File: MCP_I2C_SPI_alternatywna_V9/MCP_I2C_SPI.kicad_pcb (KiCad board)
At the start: 2 copper layers, 97.7 x 99.8 mm, 42 parts, among them J1 GPA, J10 VCC, J11 GND, J12 I2C, J13 Interrupt0, J14 A2, J15 A1, J16 A0, J17 SDA, J18 SCK, J19 INTA, J2 GPB, J20 INTB, J21 V0, J22 Ext, J23 SPI, J24 InterruptS, J25 A2, J27 GPB, J28 GPA, J29 A1, J3 Data, J31 A0, J32 INTA, J33 INTB, J4 Control, J5 Zlacze_LCD, J6 VSS, J65 SIL7, J66 SIL5, J7 K, J8 VDD, J9 A, U1 MCP23017_SP, U2 MCP23017_SP

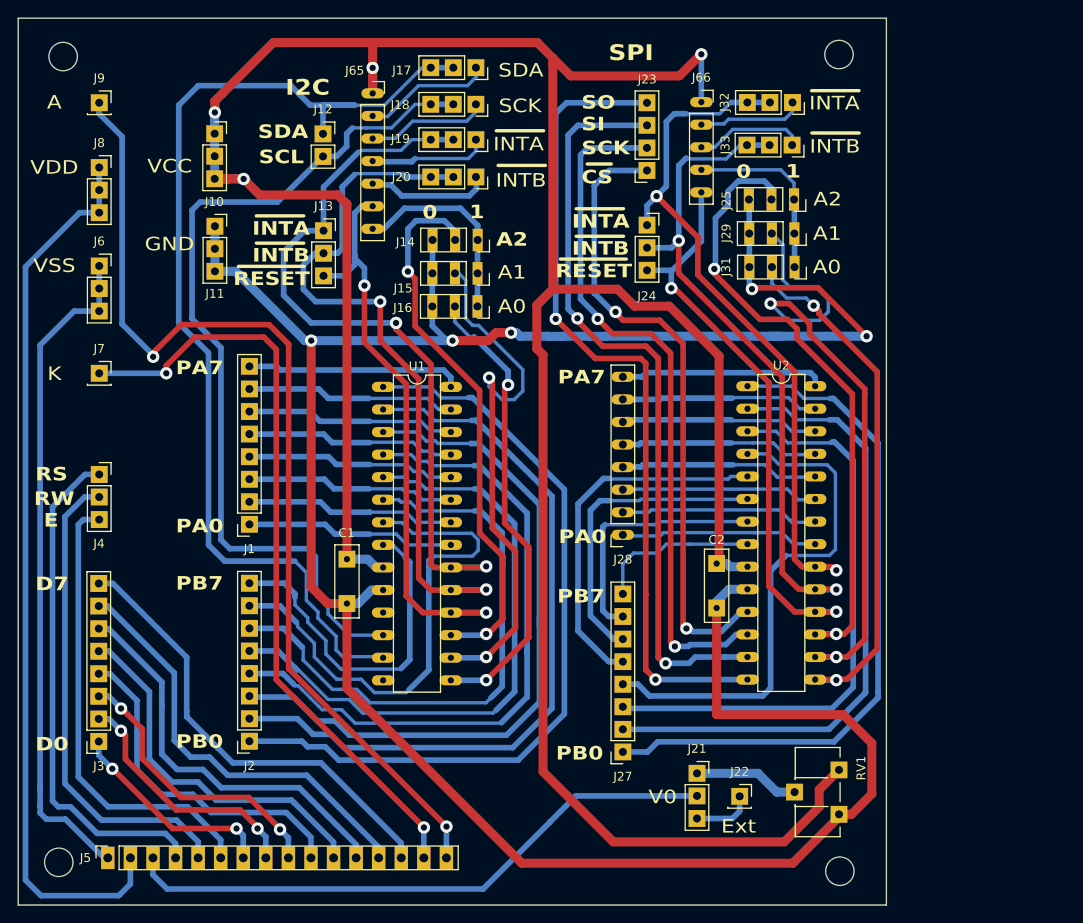
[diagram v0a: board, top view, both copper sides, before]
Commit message: MCP_I2C_SPI PCB V9
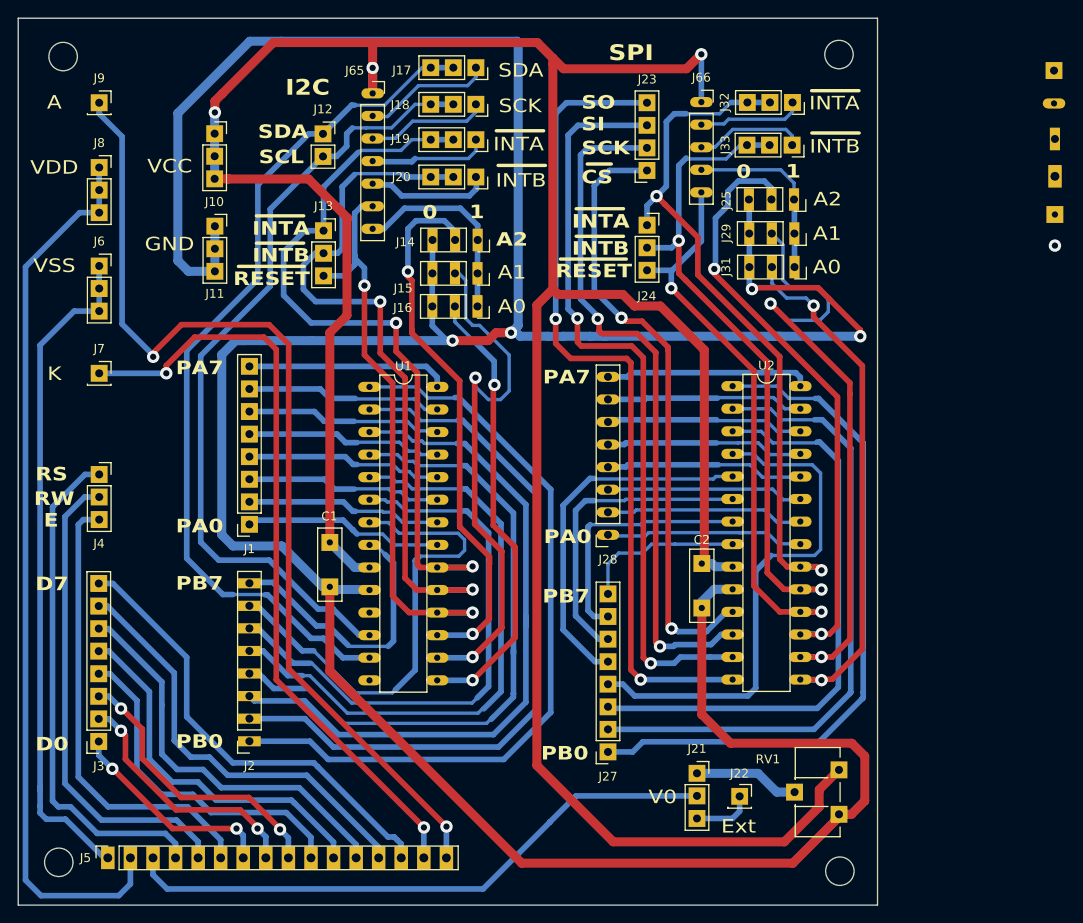
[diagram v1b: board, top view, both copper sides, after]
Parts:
- added ?: , , F.Cu at (168.6, 38.3)
- added ?: , , F.Cu at (168.6, 34.1)
- added ?: , , F.Cu at (168.6, 42.6)
- added ?: , , F.Cu at (168.5, 26.4)
- added ?: , , F.Cu at (168.5, 30.1)
- moved C1 2.70 mm to (87.0, 79.5)
- moved C2 1.67 mm to (128.9, 81.9)
- moved J27 1.67 mm to (118.3, 103.1)
- moved J28 1.67 mm to (118.3, 78.6)
- moved U2 1.67 mm to (132.3, 61.9)
- moved U1 1.53 mm to (91.5, 62.0)
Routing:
- net GND: track 280.5 -> 375.8 mm, vias 5 -> 4
- net SDA: track 121.9 -> 98.8 mm
- net SCL: track 99.3 -> 90.4 mm
- net Net-(J2-Pin_8): track 38.2 -> 31.9 mm
- net +5V: track 318.0 -> 311.9 mm, vias 4 -> 3
- net Net-(J2-Pin_7): track 57.5 -> 54.9 mm
- net Net-(J25-Pin_2): track 72.1 -> 69.6 mm
- net Net-(J2-Pin_6): track 65.7 -> 63.4 mm
- net CS: track 71.3 -> 69.1 mm
- net Net-(J2-Pin_5): track 70.4 -> 68.3 mm
- net Net-(J29-Pin_2): track 73.0 -> 71.1 mm
- net Net-(J2-Pin_1): track 88.9 -> 87.3 mm
- net Net-(J2-Pin_2): track 84.2 -> 82.6 mm
- net Net-(J2-Pin_3): track 80.2 -> 78.6 mm
- net Net-(J1-Pin_3): track 23.6 -> 22.1 mm
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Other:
- board size 97.7 x 99.8 mm -> 96.7 x 99.8 mm
- board text added: "Goldpin 100x45mils (2,54x1,143mm) fi=0,9mm (35,43mils)"
- board text added: "Goldpin 75x75mils (1,905x1,905mm) fi=0,9mm (35,43mils)"
- board text added: "Kondensator 75x75mils (1,905x1,905mm) fi=0,7mm (27,55mils)"
- board text added: "Przelotka średnica=55mils (1,397mm) fi=0,7mm (27,55mils)"
- board text added: "SIL 100x45mils (2,54x1,143mm) fi=0,7mm (27,55mils)"
- board text added: "Wyswietlacz 100x60mils (2,54x1,524mm) fi=1mm (39,37mils)"
